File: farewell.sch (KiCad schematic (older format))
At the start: 27 parts, among them SW1 SW_Push, U1 0

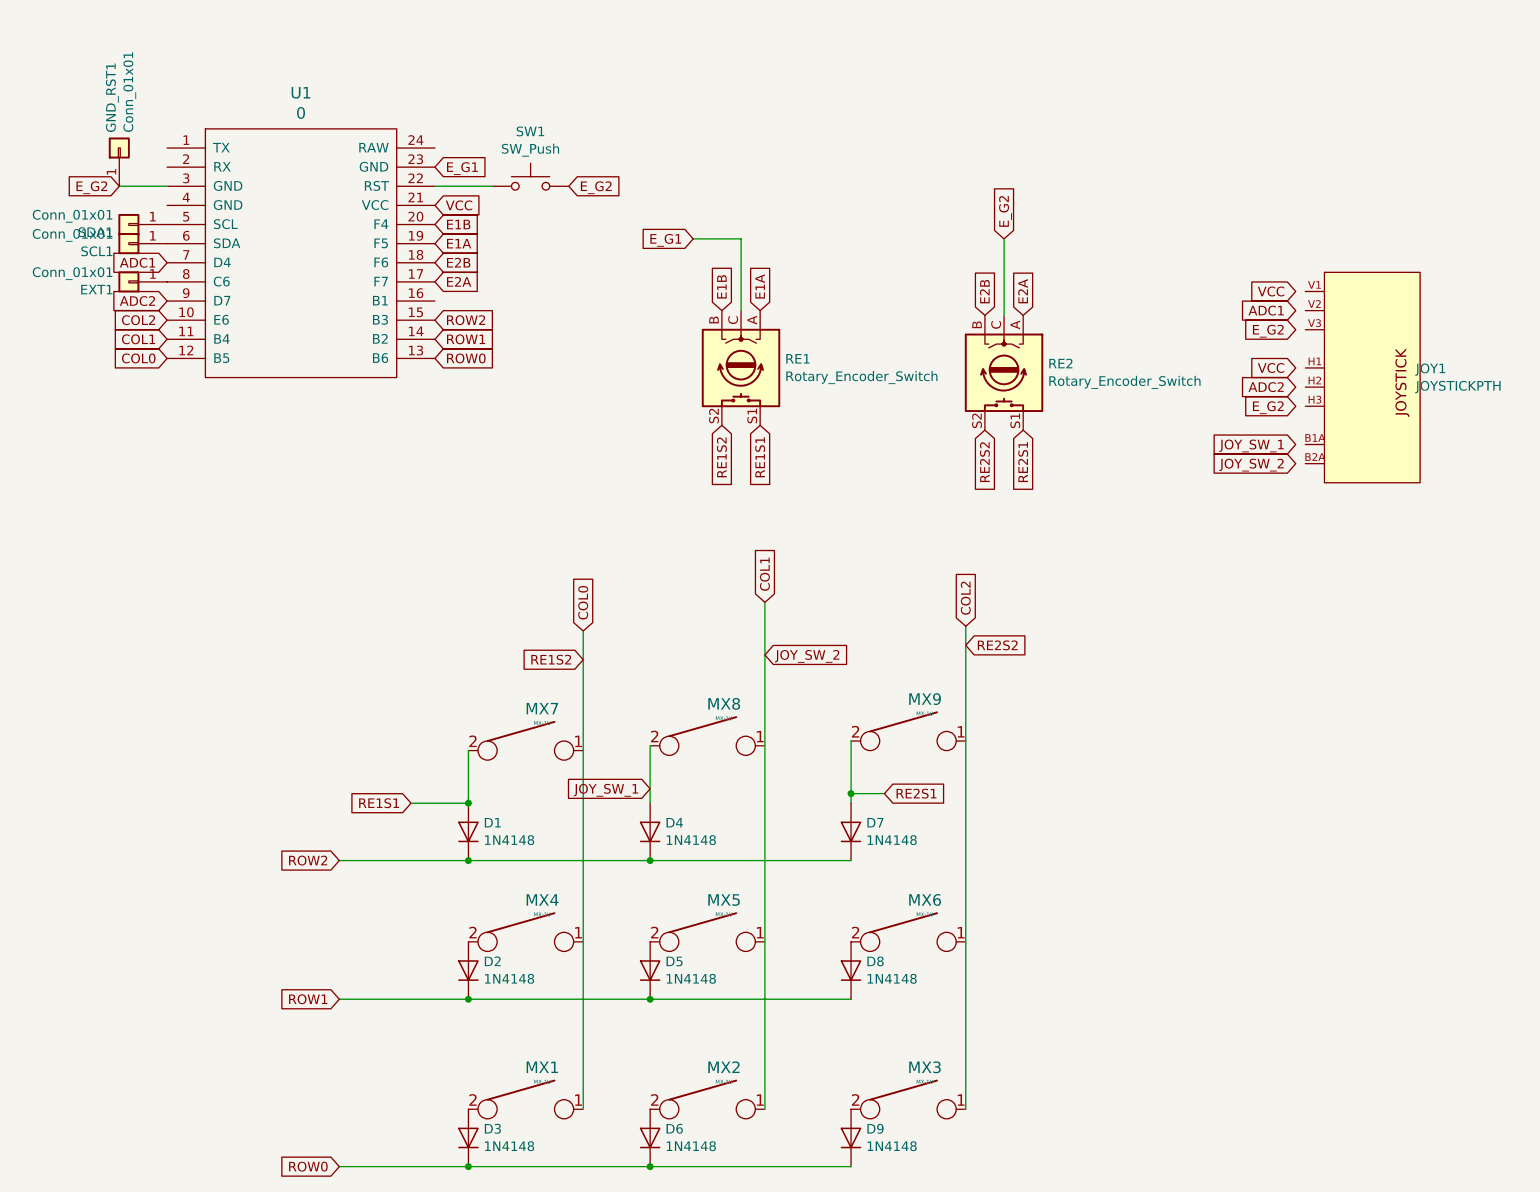
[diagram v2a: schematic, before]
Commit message: V2 fixes + WS2812 holes in pcb
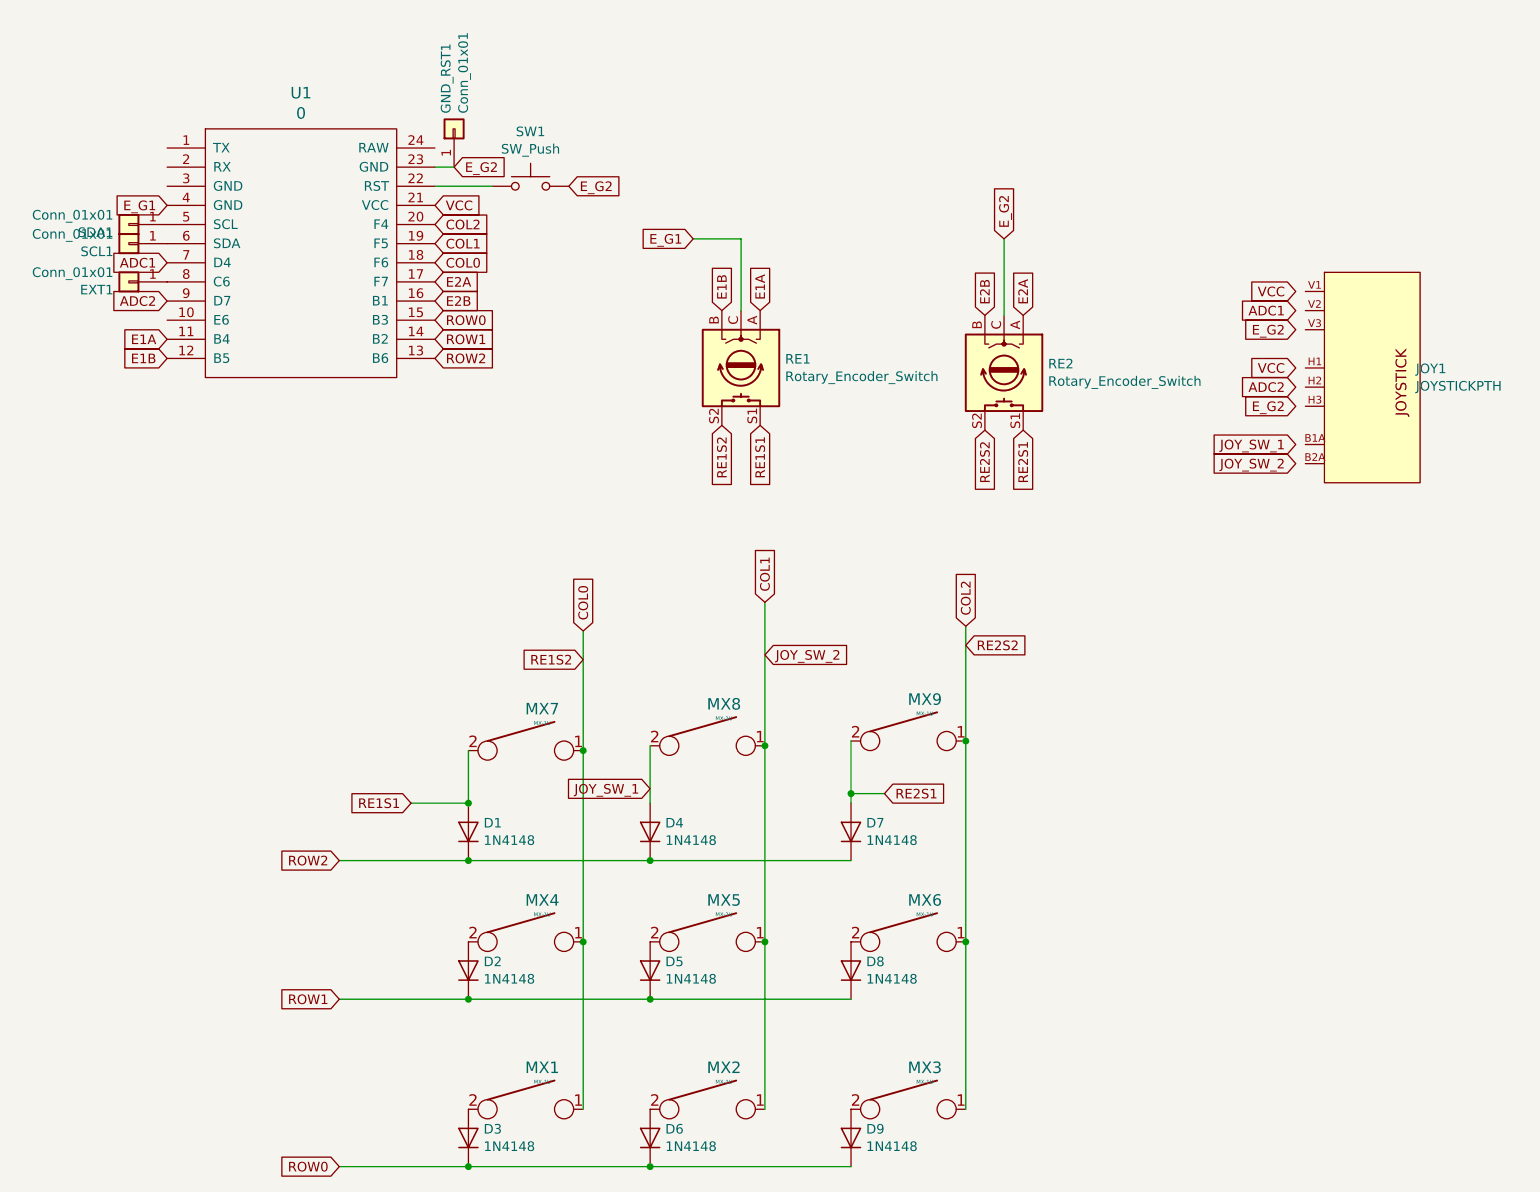
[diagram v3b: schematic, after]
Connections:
- net COL0: now also MX4.1, MX7.1, U1.18 (F6); no longer U1.12 (B5)
- net COL1: now also MX5.1, MX8.1, U1.19 (F5); no longer U1.11 (B4)
- net COL2: now also MX6.1, MX9.1, U1.20 (F4); no longer U1.10 (E6)
- net E1A: now also U1.11 (B4); no longer U1.19 (F5)
- net E1B: now also U1.12 (B5); no longer U1.20 (F4)
- net E2B: now also U1.16 (B1); no longer U1.18 (F6)
- net E_G1: now also U1.4 (GND); no longer U1.23 (GND)
- net E_G2: now also U1.23 (GND); no longer U1.3 (GND)
- net ROW0: now also U1.15 (B3); no longer U1.13 (B6)
- net ROW2: now also U1.13 (B6); no longer U1.15 (B3)
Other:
- moved on the sheet: GND_RST1
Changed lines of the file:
@@
 EESchema Schematic File Version 4
-LIBS:farewell-cache
-EELAYER 29 0
+EELAYER 30 0
 EELAYER END
 $Descr A4 11693 8268
@@
 $EndDescr
 $Comp
-L keyboard-parts2:KEYSW MX1
-U 1 1 5C9FFB86
-P 2975 6675
-F 0 "MX1" H 3061 6892 60  0000 C CNN
-F 1 "MX-1U" H 3061 6818 20  0000 C CNN
-F 2 "farewell:MX-1U-NoLED-NoPCBMount" H 2950 6650 60  0001 C CNN
-F 3 "" H 2950 6650 60  0001 C CNN
-	1    2975 6675
-	1    0    0    -1
-$EndComp
-$Comp
 L keyboard-parts2:KEYSW MX2
 U 1 1 5CA014D4
@@
 F 3 "" H 4950 6650 60  0001 C CNN
 	1    4975 6675
-	1    0    0    -1
-$EndComp
-$Comp
-L keyboard-parts2:KEYSW MX4
-U 1 1 5CA0561D
-P 2975 5800
-F 0 "MX4" H 3061 6017 60  0000 C CNN
-F 1 "MX-1U" H 3061 5943 20  0000 C CNN
-F 2 "farewell:MX-1U-NoLED-NoPCBMount" H 2950 5775 60  0001 C CNN
-F 3 "" H 2950 5775 60  0001 C CNN
-	1    2975 5800
 	1    0    0    -1
 $EndComp
@@
 $EndComp
 $Comp
-L Diode:1N4148 D3
-U 1 1 5CA29486
-P 2675 6825
-F 0 "D3" V 2721 6746 50  0000 R CNN
-F 1 "1N4148" V 2630 6746 50  0000 R CNN
-F 2 "keyboard_parts:D_SOD123_axial" H 2675 6650 50  0001 C CNN
-F 3 "https://assets.nexperia.com/documents/data-sheet/1N4148_1N4448.pdf" H 2675 6825 50  0001 C CNN
-	1    2675 6825
-	0    -1   -1   0
-$EndComp
-$Comp
 L Diode:1N4148 D2
 U 1 1 5CA39A7D
@@
 Wire Wire Line
 	2675 5375 2000 5375
-Text GLabel 3275 4175 1    50   Input ~ 0
-COL0
-Text GLabel 4225 4025 1    50   Input ~ 0
-COL1
 Text GLabel 5275 4150 1    50   Input ~ 0
 COL2
@@
 Text GLabel 2500 2350 2    50   Input ~ 0
 E2A
-Text GLabel 2500 2250 2    50   Input ~ 0
+Text GLabel 2500 2450 2    50   Input ~ 0
 E2B
-Text GLabel 2500 2150 2    50   Input ~ 0
-E1A
-Text GLabel 2500 2050 2    50   Input ~ 0
+Text GLabel 1100 2750 0    50   Input ~ 0
 E1B
-Text GLabel 2500 2550 2    50   Input ~ 0
-ROW2
 Text GLabel 2500 2650 2    50   Input ~ 0
 ROW1
@@
 	4675 6100 3625 6100
 Connection ~ 3625 6100
-Wire Wire Line
-	2675 6975 3625 6975
-$Comp
-L promicro:ProMicro U1
-U 1 1 5CB5D06D
-P 1800 2400
-F 0 "U1" H 1800 3437 60  0000 C CNN
-F 1 "0" H 1800 3331 60  0000 C CNN
-F 2 "promicro:ProMicro" H 1900 1350 60  0001 C CNN
-F 3 "" H 1900 1350 60  0000 C CNN
-	1    1800 2400
-	1    0    0    -1
-$EndComp
 Connection ~ 2675 6100
 Wire Wire Line
@@
 Text GLabel 5275 4250 2    50   Input ~ 0
 RE2S2
-Text GLabel 1100 2550 0    50   Input ~ 0
-COL2
-Text GLabel 1100 2650 0    50   Input ~ 0
+Text GLabel 2500 2150 2    50   Input ~ 0
 COL1
-Text GLabel 1100 2750 0    50   Input ~ 0
+Text GLabel 2500 2250 2    50   Input ~ 0
 COL0
 Text GLabel 5475 2125 1    50   Input ~ 0
 E_G2
-Text GLabel 850  1850 0    50   Input ~ 0
+Text GLabel 2600 1750 2    50   Input ~ 0
 E_G2
 Wire Wire Line
 	3625 6975 4675 6975
 Connection ~ 3625 6975
-Wire Wire Line
-	2675 6975 2000 6975
-Connection ~ 2675 6975
 Text GLabel 2000 6975 0    50   Input ~ 0
 ROW0
-Text GLabel 2500 2750 2    50   Input ~ 0
+Text GLabel 2500 2550 2    50   Input ~ 0
 ROW0
 Connection ~ 3625 5375
@@
 L Connector_Generic:Conn_01x01 GND_RST1
 U 1 1 5CA6404D
-P 850 1650
-F 0 "GND_RST1" H 930 1692 50  0000 L CNN
-F 1 "Conn_01x01" H 930 1601 50  0000 L CNN
-F 2 "keyboard_parts:PIN_1" H 850 1650 50  0001 C CNN
-F 3 "~" H 850 1650 50  0001 C CNN
-	1    850  1650
+P 2600 1550
+F 0 "GND_RST1" H 2680 1592 50  0000 L CNN
+F 1 "Conn_01x01" H 2680 1501 50  0000 L CNN
+F 2 "keyboard_parts:PIN_1" H 2600 1550 50  0001 C CNN
+F 3 "~" H 2600 1550 50  0001 C CNN
+	1    2600 1550
 	0    -1   -1   0
 $EndComp
@@
 F 3 "~" H 900 2050 50  0001 C CNN
 	1    900  2050
-	-1   0    0    1
-$EndComp
-$Comp
-L Connector_Generic:Conn_01x01 EXT1
-U 1 1 5CAA7D24
-P 900 2350
-F 0 "EXT1" H 980 2392 50  0000 L CNN
-F 1 "Conn_01x01" H 980 2301 50  0000 L CNN
-F 2 "keyboard_parts:PIN_1" H 900 2350 50  0001 C CNN
-F 3 "~" H 900 2350 50  0001 C CNN
-	1    900  2350
 	-1   0    0    1
 $EndComp
@@
 Text GLabel 4225 4300 2    50   Input ~ 0
 JOY_SW_2
-Wire Wire Line
-	1100 1850 850  1850
-Text GLabel 2500 1750 2    50   Input ~ 0
+Text GLabel 1100 1950 0    50   Input ~ 0
 E_G1
 $Comp
@@
 E_G2
 Wire Wire Line
-	5275 4150 5275 6675
-Wire Wire Line
-	3275 4175 3275 6675
-Wire Wire Line
-	4225 4025 4225 6675
+	2500 1750 2600 1750
+$Comp
+L keyboard-parts2:KEYSW MX4
+U 1 1 5CA0561D
+P 2975 5800
+F 0 "MX4" H 3061 6017 60  0000 C CNN
+F 1 "MX-1U" H 3061 5943 20  0000 C CNN
+F 2 "farewell:MX-1U-NoLED-NoPCBMount" H 2950 5775 60  0001 C CNN
+F 3 "" H 2950 5775 60  0001 C CNN
+	1    2975 5800
+	1    0    0    -1
+$EndComp
+Connection ~ 2675 6975
+Wire Wire Line
+	2675 6975 2000 6975
+Wire Wire Line
+	2675 6975 3625 6975
+$Comp
+L Diode:1N4148 D3
+U 1 1 5CA29486
+P 2675 6825
+F 0 "D3" V 2721 6746 50  0000 R CNN
+F 1 "1N4148" V 2630 6746 50  0000 R CNN
+F 2 "keyboard_parts:D_SOD123_axial" H 2675 6650 50  0001 C CNN
+F 3 "https://assets.nexperia.com/documents/data-sheet/1N4148_1N4448.pdf" H 2675 6825 50  0001 C CNN
+	1    2675 6825
+	0    -1   -1   0
+$EndComp
+$Comp
+L keyboard-parts2:KEYSW MX1
+U 1 1 5C9FFB86
+P 2975 6675
+F 0 "MX1" H 3061 6892 60  0000 C CNN
+F 1 "MX-1U" H 3061 6818 20  0000 C CNN
+F 2 "farewell:MX-1U-NoLED-NoPCBMount" H 2950 6650 60  0001 C CNN
+F 3 "" H 2950 6650 60  0001 C CNN
+	1    2975 6675
+	1    0    0    -1
+$EndComp
+Text GLabel 4225 4025 1    50   Input ~ 0
+COL1
+Text GLabel 3275 4175 1    50   Input ~ 0
+COL0
+Wire Wire Line
+	3275 4175 3275 4800
+Connection ~ 3275 4800
+Wire Wire Line
+	3275 4800 3275 5800
+Connection ~ 3275 5800
+Wire Wire Line
+	3275 5800 3275 6675
+Wire Wire Line
+	4225 4025 4225 4775
+Connection ~ 4225 4775
+Wire Wire Line
+	4225 4775 4225 5800
+Connection ~ 4225 5800
+Wire Wire Line
+	4225 5800 4225 6675
+Wire Wire Line
+	5275 4150 5275 4750
+Connection ~ 5275 4750
+Wire Wire Line
+	5275 4750 5275 5800
+Connection ~ 5275 5800
+Wire Wire Line
+	5275 5800 5275 6675
+Text GLabel 2500 2050 2    50   Input ~ 0
+COL2
+Text GLabel 2500 2750 2    50   Input ~ 0
+ROW2
+Text GLabel 1100 2650 0    50   Input ~ 0
+E1A
+$Comp
+L Connector_Generic:Conn_01x01 EXT1
+U 1 1 5CAA7D24
+P 900 2350
+F 0 "EXT1" H 980 2392 50  0000 L CNN
+F 1 "Conn_01x01" H 980 2301 50  0000 L CNN
+F 2 "keyboard_parts:PIN_1" H 900 2350 50  0001 C CNN
+F 3 "~" H 900 2350 50  0001 C CNN
+	1    900  2350
+	-1   0    0    1
+$EndComp
+$Comp
+L promicro:ProMicro U1
+U 1 1 5CB5D06D
+P 1800 2400
+F 0 "U1" H 1800 3437 60  0000 C CNN
+F 1 "0" H 1800 3331 60  0000 C CNN
+F 2 "promicro:ProMicro" H 1900 1350 60  0001 C CNN
+F 3 "" H 1900 1350 60  0000 C CNN
+	1    1800 2400
+	1    0    0    -1
+$EndComp
 $EndSCHEMATC
